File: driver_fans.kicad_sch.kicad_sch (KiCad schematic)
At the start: 10 parts, among them Q3 2N7002, U1 EL3H7

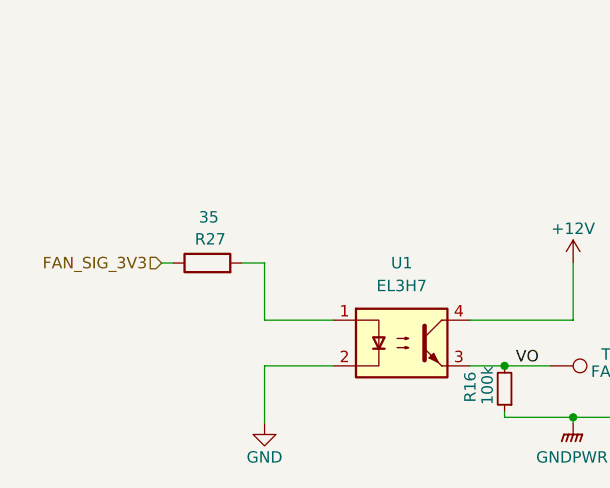
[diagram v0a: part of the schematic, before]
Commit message: Changed optocoupler resistor values, updated Mouser PNs
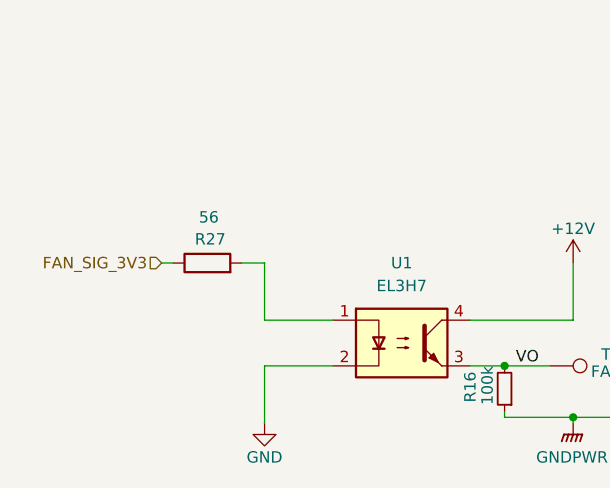
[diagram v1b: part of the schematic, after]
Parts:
- D10, D7: Mauser PN 637-1N4148WS -> (none); Mouser PN (none) -> 637-1N4148WS
- FAN1, FAN2: Mauser PN 538-43650-0415 -> (none); Mouser PN (none) -> 538-43650-0415
- Q3: Mauser PN 771-2N7002HR -> (none); Mouser PN (none) -> 771-2N7002HR
- R16: Mauser PN 71-CRCW0805100KFKEAC -> (none); Mouser PN (none) -> 71-CRCW0805100KFKEAC
- R27: value 35 -> 56; Mauser PN 791-WR08X35R2FTL -> (none); Mouser PN (none) -> 71-CRCW080556R0FKEAC; PN WR08X35R2FTL -> CRCW080556R0FKEAC
- U1: Mauser PN 638-EL3H7DTAVG -> (none); Mouser PN (none) -> 638-EL3H7DTAVG
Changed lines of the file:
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@@
       (effects (font (size 1.27 1.27)) hide)
     )
-    (property "Mauser PN" "538-43650-0415" (at 185.42 88.9 0)
+    (property "Mouser PN" "538-43650-0415" (at 185.42 88.9 0)
       (effects (font (size 1.27 1.27)) hide)
     )
@@
       (effects (font (size 1.27 1.27)) hide)
     )
-    (property "Mauser PN" "71-CRCW0805100KFKEAC" (at 95.25 104.14 0)
+    (property "Mouser PN" "71-CRCW0805100KFKEAC" (at 95.25 104.14 0)
       (effects (font (size 1.27 1.27)) hide)
     )
@@
       (effects (font (size 1.27 1.27)) (justify left))
     )
-    (property "Value" "35" (at 63.5 85.09 90)
+    (property "Value" "56" (at 63.5 85.09 90)
       (effects (font (size 1.27 1.27)) (justify left))
     )
@@
       (effects (font (size 1.27 1.27)) hide)
     )
-    (property "Datasheet" "https://www.mouser.com/datasheet/2/210/ASC_WR-3314721.pdf" (at 62.23 90.17 0)
-      (effects (font (size 1.27 1.27)) hide)
-    )
-    (property "PN" "WR08X35R2FTL" (at 62.23 90.17 0)
-      (effects (font (size 1.27 1.27)) hide)
-    )
-    (property "Mauser PN" "791-WR08X35R2FTL" (at 62.23 90.17 0)
+    (property "Datasheet" "https://www.vishay.com/docs/28773/crcwce3.pdf" (at 62.23 90.17 0)
+      (effects (font (size 1.27 1.27)) hide)
+    )
+    (property "PN" "CRCW080556R0FKEAC" (at 62.23 90.17 0)
+      (effects (font (size 1.27 1.27)) hide)
+    )
+    (property "Mouser PN" "71-CRCW080556R0FKEAC" (at 62.23 90.17 0)
       (effects (font (size 1.27 1.27)) hide)
     )
@@
       (effects (font (size 1.27 1.27)) hide)
     )
-    (property "Mauser PN" "771-2N7002HR" (at 120.65 97.79 0)
+    (property "Mouser PN" "771-2N7002HR" (at 120.65 97.79 0)
       (effects (font (size 1.27 1.27)) hide)
     )
@@
       (effects (font (size 1.27 1.27)) (justify left) hide)
     )
-    (property "Mauser PN" "638-EL3H7DTAVG " (at 83.82 99.06 0)
-      (effects (font (size 1.27 1.27)) hide)
-    )
     (property "PN" "EL3H7(D)(TA)-VG" (at 83.82 99.06 0)
+      (effects (font (size 1.27 1.27)) hide)
+    )
+    (property "Mouser PN" "638-EL3H7DTAVG " (at 83.82 99.06 0)
       (effects (font (size 1.27 1.27)) hide)
     )
@@
       (effects (font (size 1.27 1.27)) hide)
     )
-    (property "Mauser PN" "771-2N7002HR" (at 142.24 97.79 0)
+    (property "Mouser PN" "771-2N7002HR" (at 142.24 97.79 0)
       (effects (font (size 1.27 1.27)) hide)
     )
@@
       (effects (font (size 1.27 1.27)) hide)
     )
-    (property "Mauser PN" "637-1N4148WS" (at 163.195 108.585 0)
+    (property "Mouser PN" "637-1N4148WS" (at 163.195 108.585 0)
       (effects (font (size 1.27 1.27)) hide)
     )
@@
       (effects (font (size 1.27 1.27)) hide)
     )
-    (property "Mauser PN" "637-1N4148WS" (at 163.195 88.265 0)
+    (property "Mouser PN" "637-1N4148WS" (at 163.195 88.265 0)
       (effects (font (size 1.27 1.27)) hide)
     )
@@
       (effects (font (size 1.27 1.27)) hide)
     )
-    (property "Mauser PN" "538-43650-0415" (at 185.42 109.22 0)
-      (effects (font (size 1.27 1.27)) hide)
-    )
+    (property "Mouser PN" "538-43650-0415" (at 185.42 109.22 0)
+      (effects (font (size 1.27 1.27)) hide)
+    )

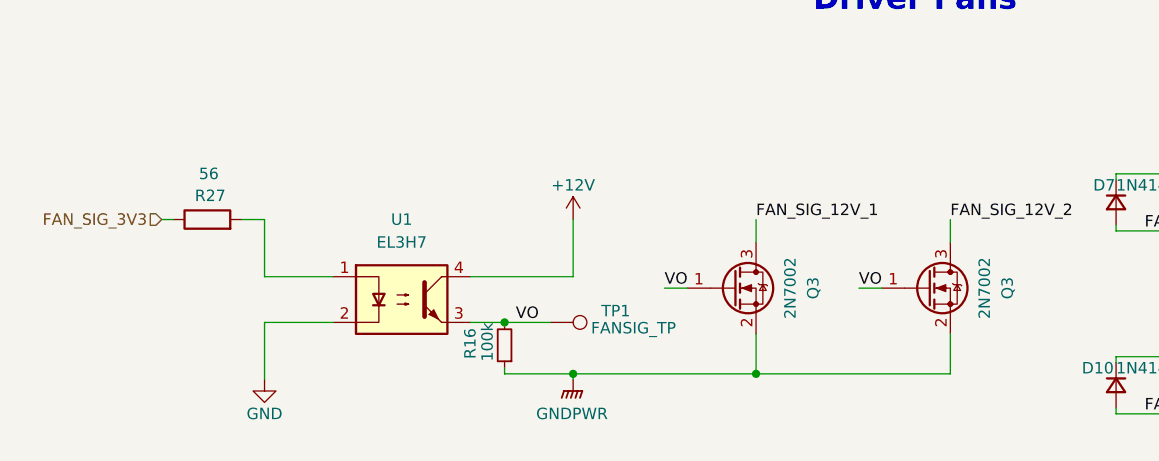
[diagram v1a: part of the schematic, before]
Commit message: Fixed leaderSOM connections, removed optocouplers for lighting and fans, found new MOSFETs
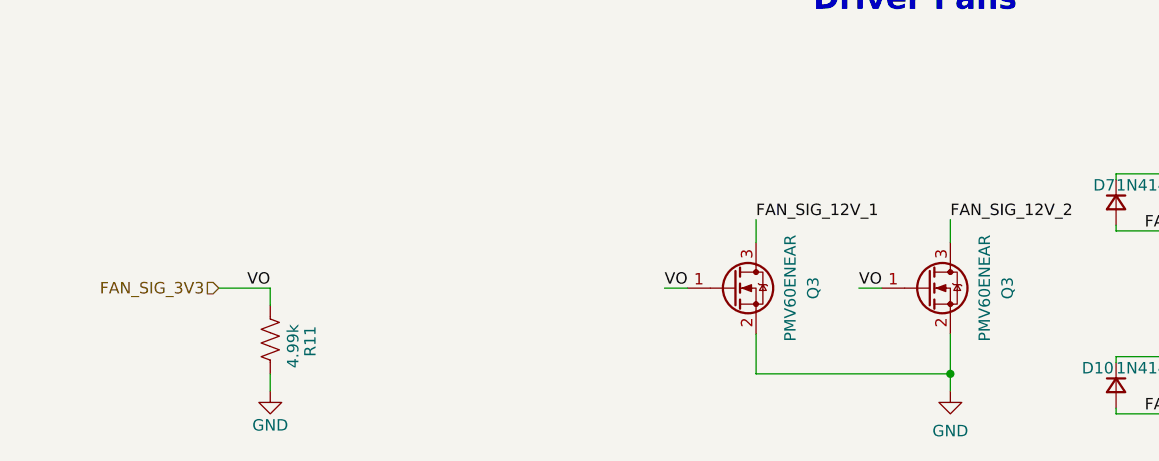
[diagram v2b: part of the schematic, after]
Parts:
- removed R16: 100k, Resistor_SMD:R_0805_2012Metric, symbol Device:R_Small
- removed R27: 56, Resistor_SMD:R_0805_2012Metric, symbol Device:R
- removed TP1: FANSIG_TP, TestPoint:TestPoint_Pad_1.5x1.5mm, symbol Connector:TestPoint
- removed U1: EL3H7, Package_SO:SOP-4_4.4x2.6mm_P1.27mm, symbol Isolator:EL817
- added R11: 4.99k, Resistor_SMD:R_0805_2012Metric, symbol Device:R_US
- Q3: value 2N7002 -> PMV60ENEAR; Mouser PN 771-2N7002HR -> 771-PMV60ENEAR; PN 2N7002HR -> PMV60ENEAR
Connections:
- net GNDPWR is gone; now on net GND: Q3.2 (S), Q3.2 (S)
- net VO is gone; now on net FAN_SIG_3V3: Q3.1 (G), Q3.1 (G)
- net FAN_SIG_3V3: now also R11.1
- net GND: now also R11.2

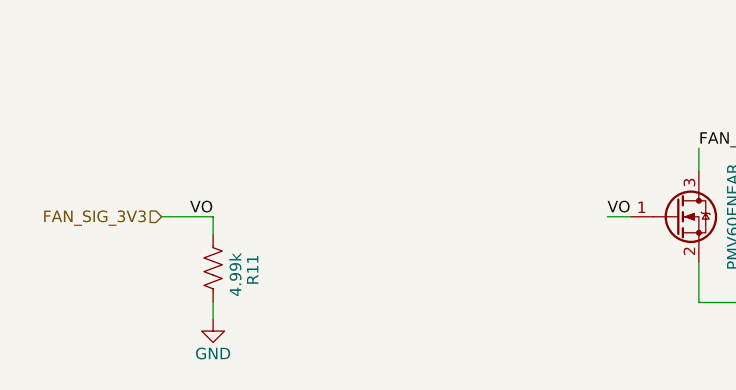
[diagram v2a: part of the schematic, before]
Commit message: Added I2C GPIO expander to reduce GPIO pins from LeaderSOM and replace 555 timer circuit. Adjusted ignition switch signals.
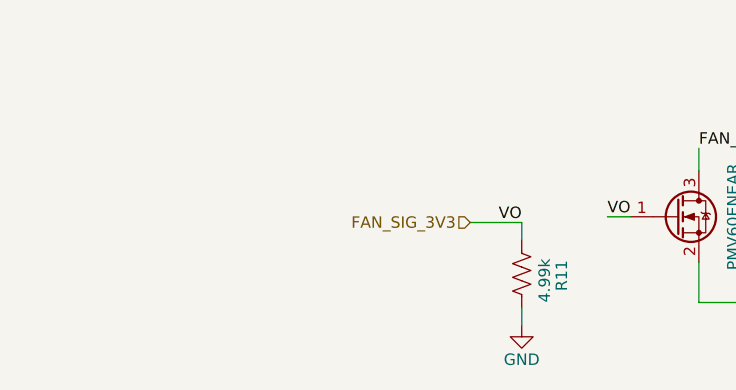
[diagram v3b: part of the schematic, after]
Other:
- moved on the sheet: R11
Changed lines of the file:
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@@
     (stroke (width 0) (type default))
   )
-  (wire (pts (xy 63.5 97.79) (xy 69.215 97.79))
+  (wire (pts (xy 97.79 98.425) (xy 103.505 98.425))
     (stroke (width 0) (type default))
   )
@@
     (stroke (width 0) (type default))
   )
-  (wire (pts (xy 69.215 97.79) (xy 69.215 99.695))
+  (wire (pts (xy 103.505 98.425) (xy 103.505 100.33))
     (stroke (width 0) (type default))
   )
@@
     (stroke (width 0) (type default))
   )
-  (wire (pts (xy 69.215 107.315) (xy 69.215 109.22))
+  (wire (pts (xy 103.505 107.95) (xy 103.505 109.855))
     (stroke (width 0) (type default))
   )
@@
     (effects (font (size 1.27 1.27)) (justify left bottom))
   )
-  (label "VO" (at 69.215 97.79 180) (fields_autoplaced)
+  (label "VO" (at 103.505 98.425 180) (fields_autoplaced)
     (effects (font (size 1.27 1.27)) (justify right bottom))
   )
@@
     (effects (font (size 1.27 1.27)) (justify left bottom))
   )
-  (hierarchical_label "FAN_SIG_3V3" (shape input) (at 63.5 97.79 180) (fields_autoplaced)
+  (hierarchical_label "FAN_SIG_3V3" (shape input) (at 97.79 98.425 180) (fields_autoplaced)
     (effects (font (size 1.27 1.27)) (justify right))
   )
@@
     )
   )
-  (symbol (lib_id "Device:R_US") (at 69.215 103.505 0) (unit 1)
-    (in_bom yes) (on_board yes) (dnp no)
-    (property "Reference" "R11" (at 73.66 105.41 90)
-      (effects (font (size 1.27 1.27)) (justify left))
-    )
-    (property "Value" "4.99k" (at 71.755 106.68 90)
-      (effects (font (size 1.27 1.27)) (justify left))
-    )
-    (property "Footprint" "Resistor_SMD:R_0805_2012Metric" (at 70.231 103.759 90)
-      (effects (font (size 1.27 1.27)) hide)
-    )
-    (property "Datasheet" "https://www.vishay.com/docs/28773/crcwce3.pdf" (at 69.215 103.505 0)
-      (effects (font (size 1.27 1.27)) hide)
-    )
-    (property "PN" "CRCW08054K99FKEAC" (at 69.215 103.505 0)
-      (effects (font (size 1.27 1.27)) hide)
-    )
-    (property "Mouser PN" "71-CRCW08054K99FKEAC " (at 69.215 103.505 0)
+  (symbol (lib_id "Device:R_US") (at 103.505 104.14 0) (unit 1)
+    (in_bom yes) (on_board yes) (dnp no)
+    (property "Reference" "R11" (at 107.95 106.045 90)
+      (effects (font (size 1.27 1.27)) (justify left))
+    )
+    (property "Value" "4.99k" (at 106.045 107.315 90)
+      (effects (font (size 1.27 1.27)) (justify left))
+    )
+    (property "Footprint" "Resistor_SMD:R_0805_2012Metric" (at 104.521 104.394 90)
+      (effects (font (size 1.27 1.27)) hide)
+    )
+    (property "Datasheet" "https://www.vishay.com/docs/28773/crcwce3.pdf" (at 103.505 104.14 0)
+      (effects (font (size 1.27 1.27)) hide)
+    )
+    (property "PN" "CRCW08054K99FKEAC" (at 103.505 104.14 0)
+      (effects (font (size 1.27 1.27)) hide)
+    )
+    (property "Mouser PN" "71-CRCW08054K99FKEAC " (at 103.505 104.14 0)
       (effects (font (size 1.27 1.27)) hide)
     )
@@
     )
   )
-  (symbol (lib_id "power:GND") (at 69.215 109.22 0) (unit 1)
-    (in_bom yes) (on_board yes) (dnp no)
-    (property "Reference" "#PWR031" (at 69.215 115.57 0)
-      (effects (font (size 1.27 1.27)) hide)
-    )
-    (property "Value" "GND" (at 69.215 113.03 0)
-      (effects (font (size 1.27 1.27)))
-    )
-    (property "Footprint" "" (at 69.215 109.22 0)
-      (effects (font (size 1.27 1.27)) hide)
-    )
-    (property "Datasheet" "" (at 69.215 109.22 0)
-      (effects (font (size 1.27 1.27)) hide)
-    )
+  (symbol (lib_id "power:GND") (at 103.505 109.855 0) (unit 1)
+    (in_bom yes) (on_board yes) (dnp no)
+    (property "Reference" "#PWR031" (at 103.505 116.205 0)
+      (effects (font (size 1.27 1.27)) hide)
+    )
+    (property "Value" "GND" (at 103.505 113.665 0)
+      (effects (font (size 1.27 1.27)))
+    )
+    (property "Footprint" "" (at 103.505 109.855 0)
+      (effects (font (size 1.27 1.27)) hide)
+    )
+    (property "Datasheet" "" (at 103.505 109.855 0)
+      (effects (font (size 1.27 1.27)) hide)
+    )

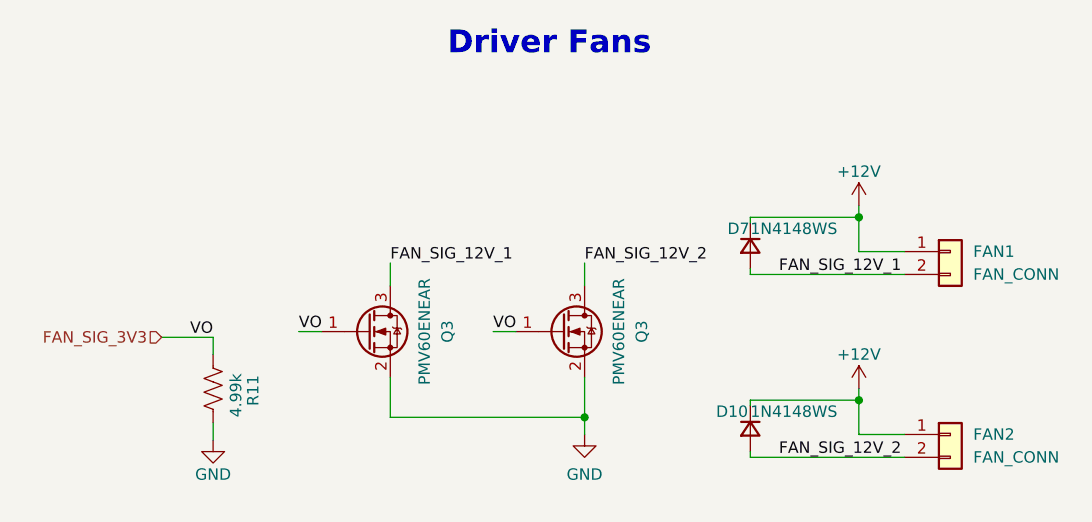
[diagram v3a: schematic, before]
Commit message: Organized schematic, removed fan MOSFET
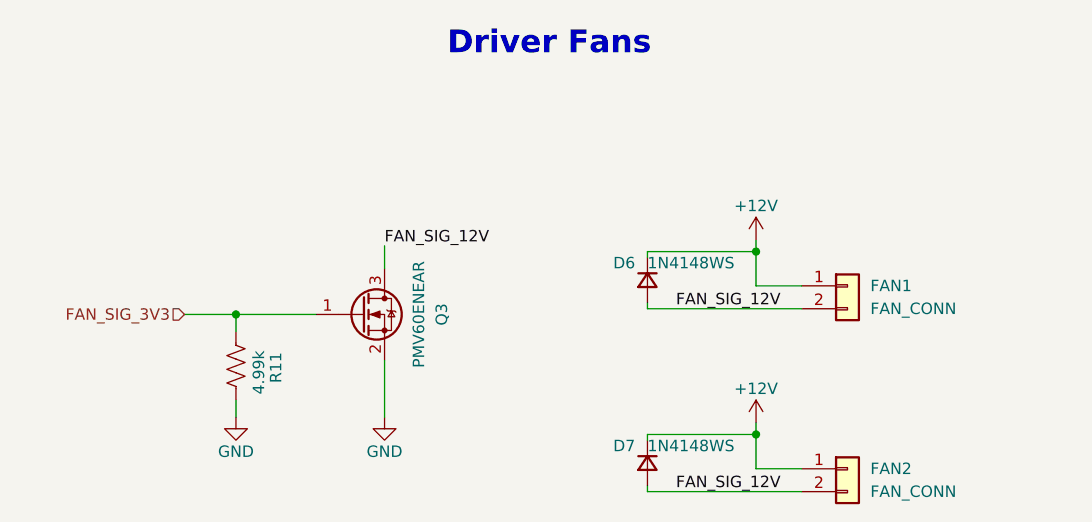
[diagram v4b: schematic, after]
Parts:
- removed D10: 1N4148WS, Diode_SMD:D_SOD-323F, symbol Device:D_Small
- removed Q3 (x2): PMV60ENEAR, Package_TO_SOT_SMD:SOT-23, symbol Transistor_FET:2N7002
- added D6: 1N4148WS, Diode_SMD:D_SOD-323F, symbol Device:D_Small
- added Q3: PMV60ENEAR, Package_TO_SOT_SMD:SOT-23, symbol Transistor_FET:2N7002
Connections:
- net FAN_SIG_12V_2 is gone; now on net FAN_SIG_12V: FAN2.2 (Pin_2)
- net +12V: now also D6.1 (K)
- net FAN_SIG_3V3: now also Q3.1 (G)
- net GND: now also Q3.2 (S)
- net FAN_SIG_12V_1 renamed FAN_SIG_12V
- net FAN_SIG_12V: now also D6.2 (A), Q3.3 (D)

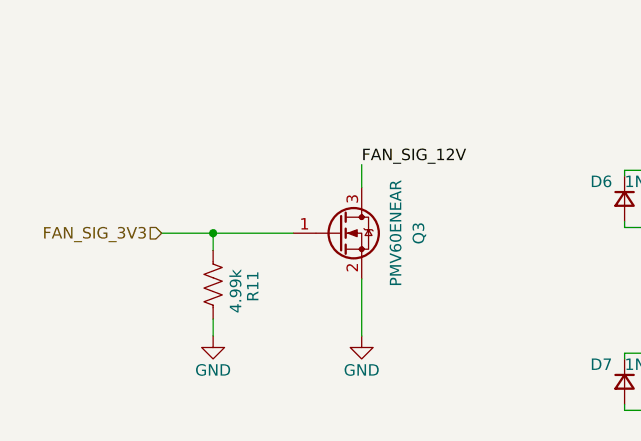
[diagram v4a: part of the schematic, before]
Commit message: organized schematic, changed resistor values, moved ignition signals to IC
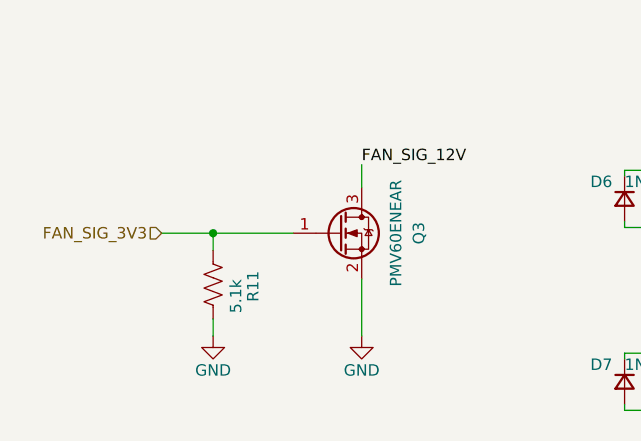
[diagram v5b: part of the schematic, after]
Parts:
- R11: value 4.99k -> 5.1k
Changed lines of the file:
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@@
       (effects (font (size 1.27 1.27)) (justify left))
     )
-    (property "Value" "4.99k" (at 108.585 104.775 90)
+    (property "Value" "5.1k" (at 108.585 104.775 90)
       (effects (font (size 1.27 1.27)) (justify left))
     )

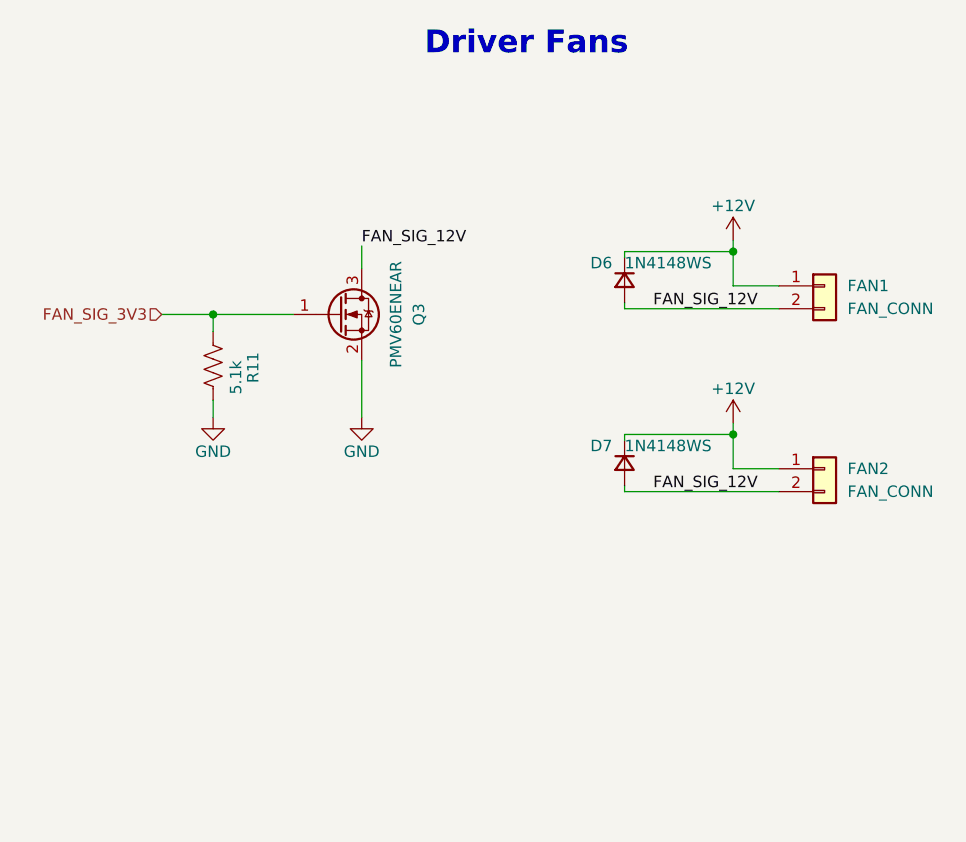
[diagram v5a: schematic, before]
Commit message: added second fan FET back
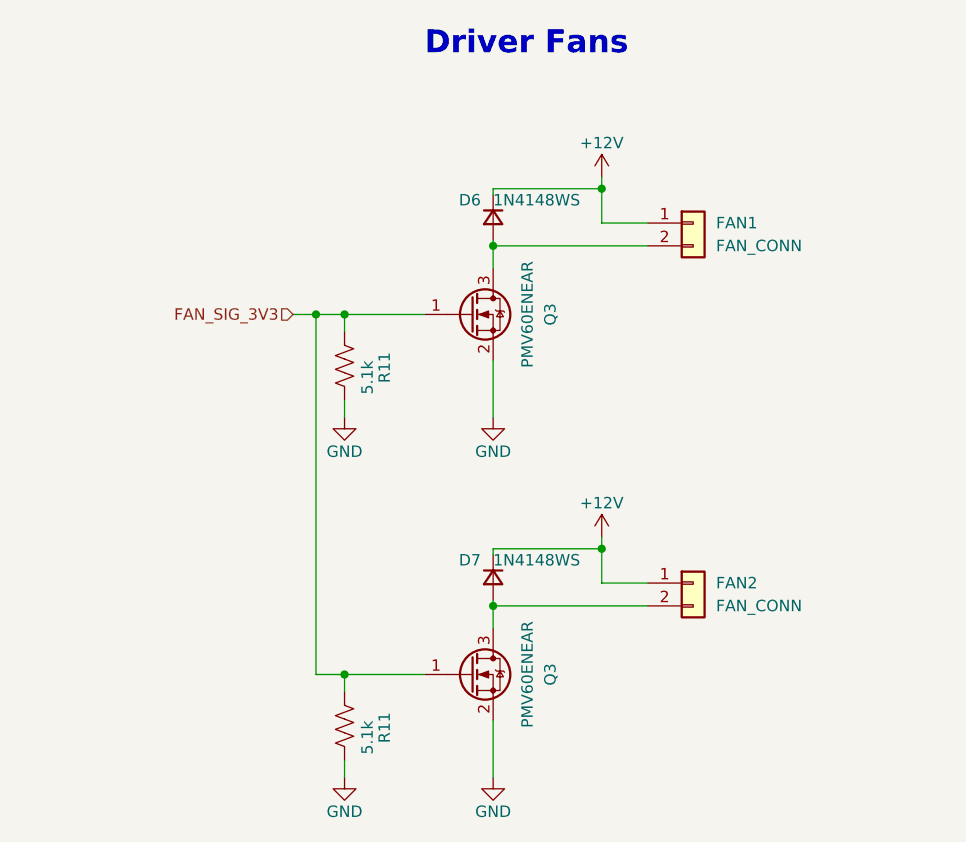
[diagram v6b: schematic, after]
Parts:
- added Q3: PMV60ENEAR, Package_TO_SOT_SMD:SOT-23, symbol Transistor_FET:2N7002
- added R11: 5.1k, Resistor_SMD:R_0805_2012Metric, symbol Device:R_US
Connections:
- net FAN_SIG_3V3: now also Q3.1 (G), R11.1
- net GND: now also Q3.2 (S), R11.2
- net FAN_SIG_12V: no longer names the net of D6.2 (A), FAN1.2 (Pin_2), Q3.3 (D)
- net FAN_SIG_12V: no longer D7.2 (A), FAN2.2 (Pin_2)
- new net: D7.2 (A), FAN2.2 (Pin_2), Q3.3 (D)
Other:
- moved on the sheet: D6, D7, FAN1, FAN2, Q3, R11
